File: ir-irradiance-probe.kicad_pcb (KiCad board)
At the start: 4 copper layers, 40 x 40 mm, 59 parts, among them J1 USB-C_UJC-HP-3-SMT-TR, J2 SM04B-SRSS-TB-LF-SN, J3 PinHeader_1x2_P2.54mm_Drill1.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, J4 Conn_BNC_031-70526-21, SW1 MSS3-V-T_R, U1 TLV70033_SC70, U2 AD8604ARUZ, U3 ADC101C027CIMK

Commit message: [47284] Add pcb sha string
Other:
- board text added: "PCB SHA ########"
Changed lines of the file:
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@@
+    (effects (font (size 0.7 0.7) (thickness 0.15)) (justify mirror))
+  )
+  (gr_text "PCB SHA ########" (at 94.39 73.78) (layer "B.SilkS")
     (effects (font (size 0.7 0.7) (thickness 0.15)) (justify mirror))
   )

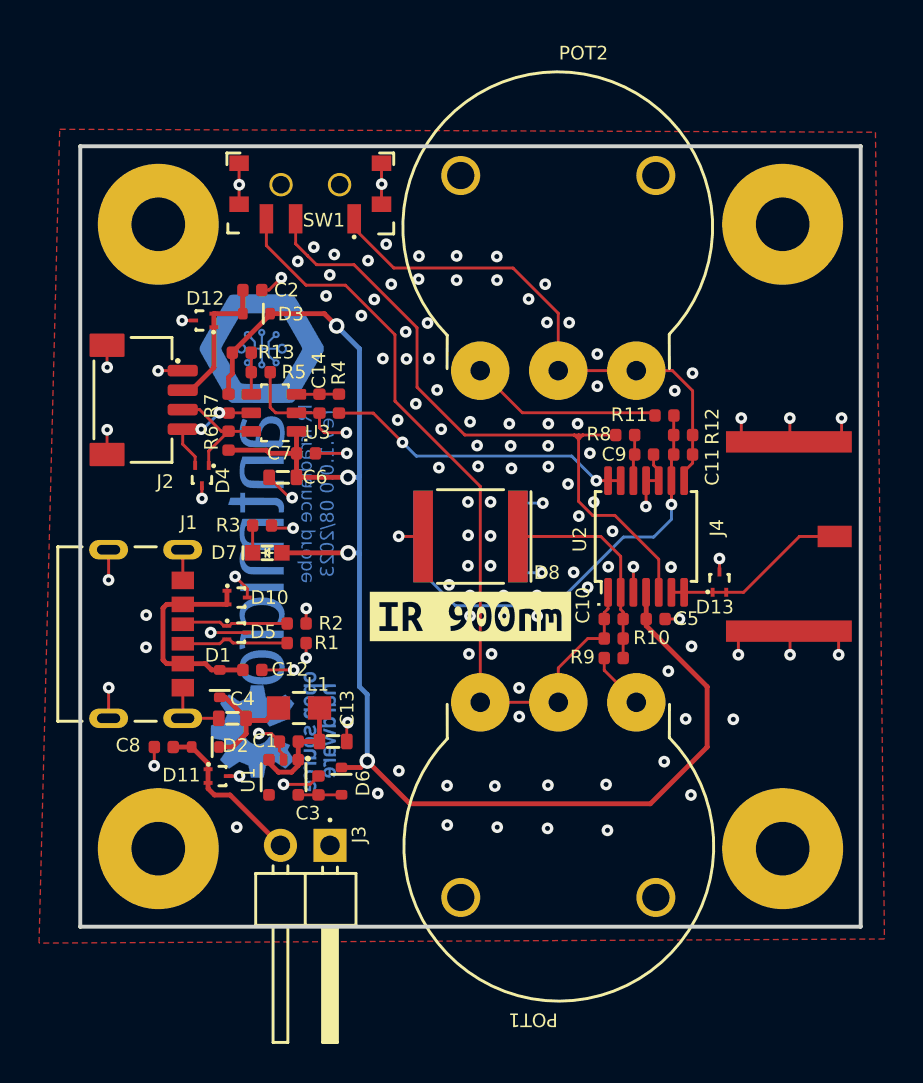
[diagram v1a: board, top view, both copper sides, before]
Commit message: [47284] Add connectors labels
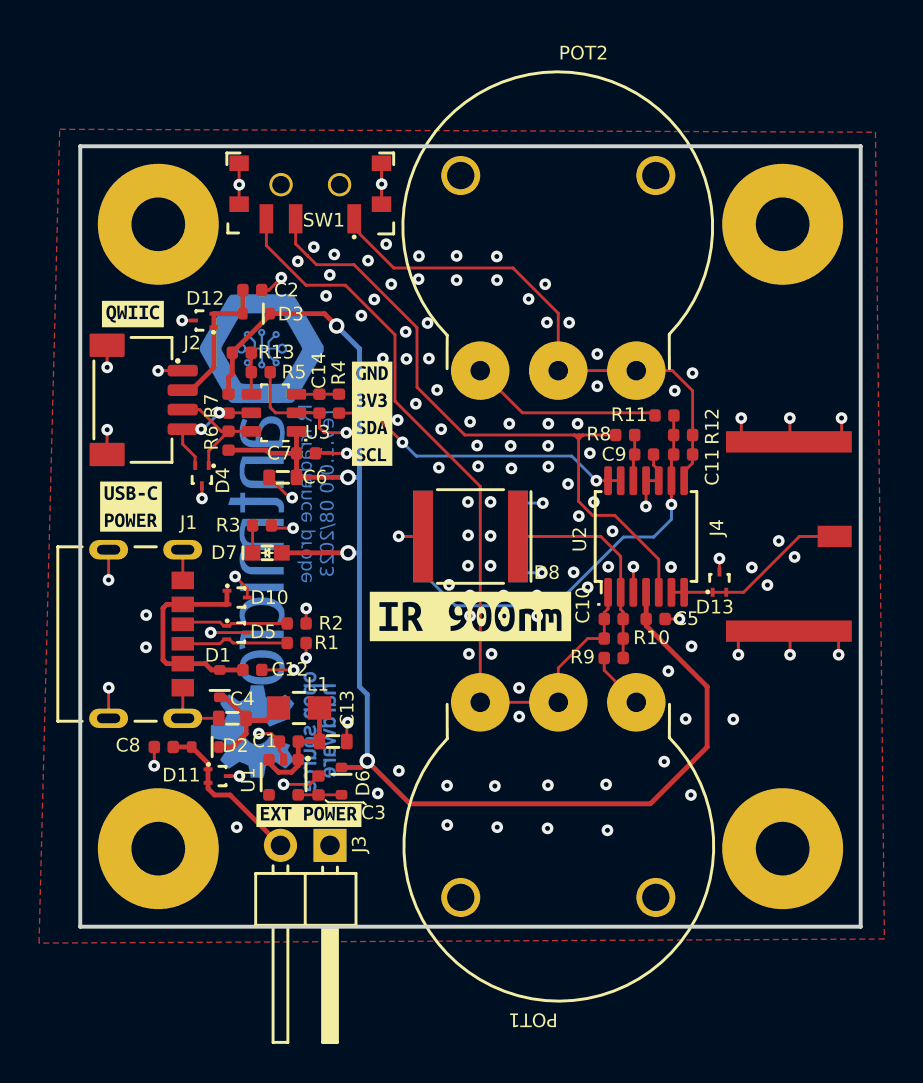
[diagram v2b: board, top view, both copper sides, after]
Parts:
- added kibuzzard-64DA12EE: G***, kibuzzard-64DA12EE, F.Cu at (72.7, 78.6)
- added kibuzzard-64DA1325: G***, kibuzzard-64DA1325, F.Cu at (72.6, 88.5)
- added kibuzzard-64DA143B: G***, kibuzzard-64DA143B, F.Cu at (81.7, 104.3)
- added kibuzzard-64DA14BC: G***, kibuzzard-64DA14BC, F.Cu at (85.0, 83.7)
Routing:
- net GND: vias 127 -> 131

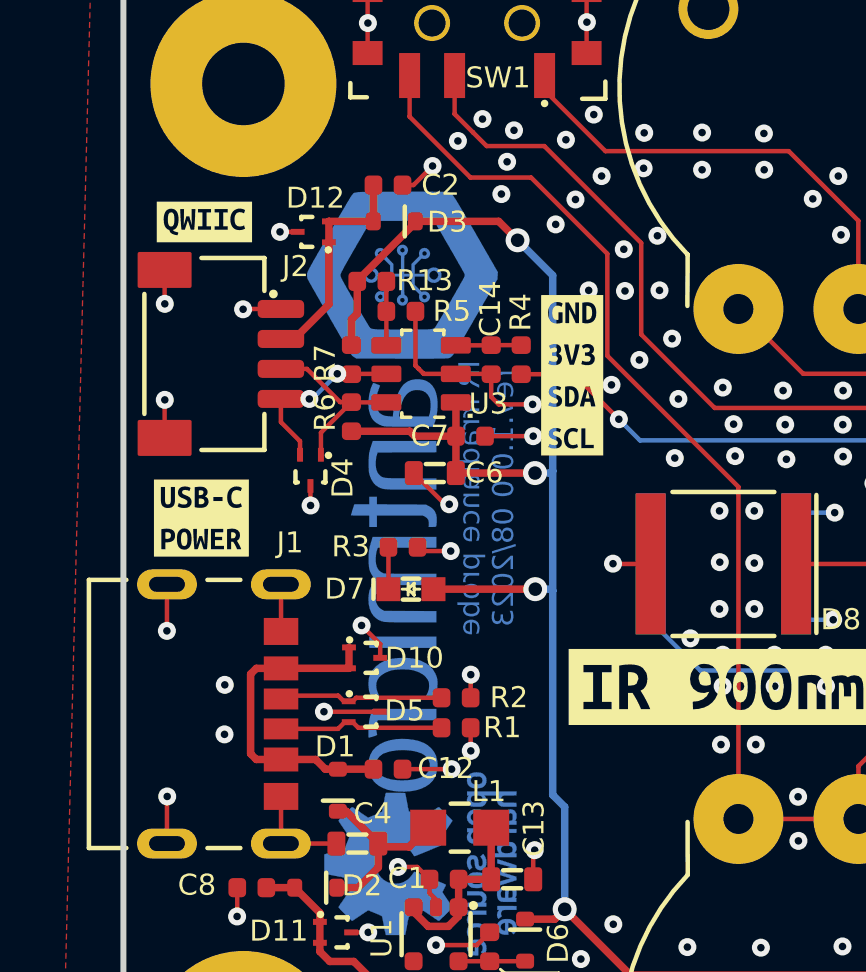
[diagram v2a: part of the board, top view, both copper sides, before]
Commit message: [#47284] Fix antmicro and ohw logos positioning
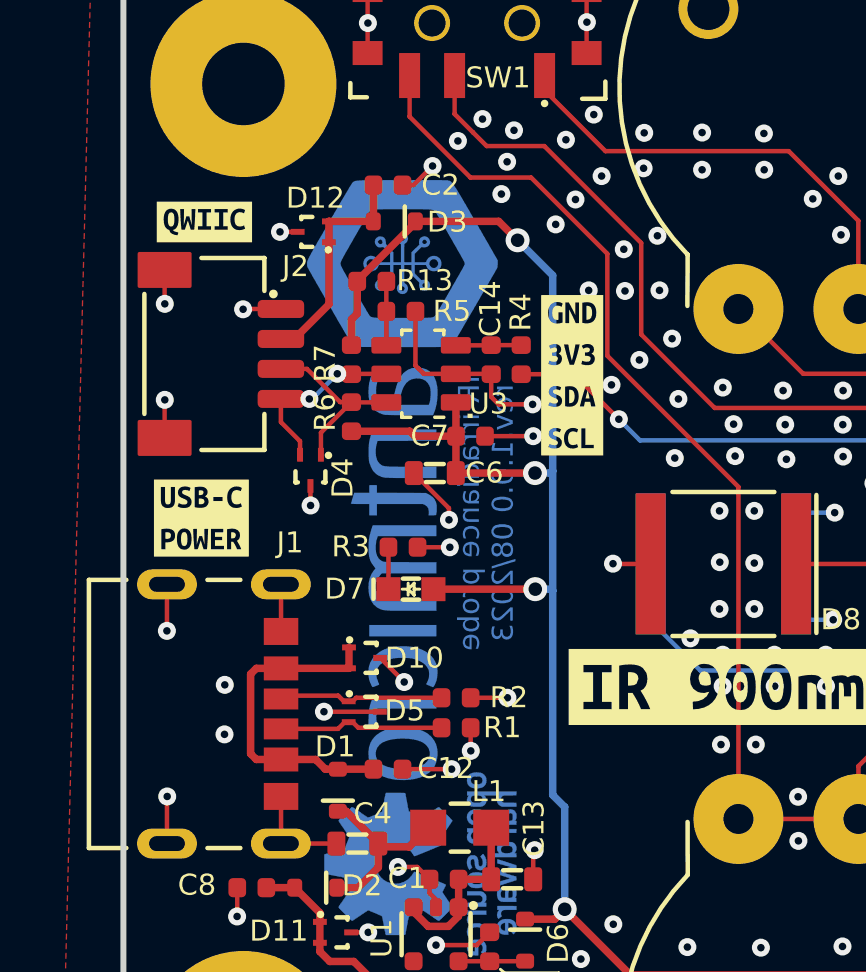
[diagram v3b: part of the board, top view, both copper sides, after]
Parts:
- moved N1 0.39 mm to (79.5, 87.2)
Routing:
- net GND: track 61.3 -> 61.9 mm
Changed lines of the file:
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@@
     (attr board_only exclude_from_pos_files exclude_from_bom)
     (fp_text reference "kibuzzard-64DA1325" (at 0 -4.332869) (layer "F.SilkS") hide
-      (effects (font (size 0 0)))
+      (effects (font (size 0 0) (thickness 0.15)))
     )
     (fp_text value "G***" (at 0 4.332869) (layer "F.SilkS") hide
-      (effects (font (size 0 0)))
+      (effects (font (size 0 0) (thickness 0.15)))
     )
     (fp_poly (pts
@@
     (attr board_only exclude_from_pos_files exclude_from_bom)
     (fp_text reference "kibuzzard-64DA12EE" (at 0 -3.725677) (layer "F.SilkS") hide
-      (effects (font (size 0 0)))
+      (effects (font (size 0 0) (thickness 0.15)))
     )
     (fp_text value "G***" (at 0 3.725677) (layer "F.SilkS") hide
-      (effects (font (size 0 0)))
+      (effects (font (size 0 0) (thickness 0.15)))
     )
     (fp_poly (pts
@@
     (attr board_only exclude_from_pos_files exclude_from_bom)
     (fp_text reference "kibuzzard-64DA143B" (at 0 -3.638444) (layer "F.SilkS") hide
-      (effects (font (size 0 0)))
+      (effects (font (size 0 0) (thickness 0.15)))
     )
     (fp_text value "G***" (at 0 3.638444) (layer "F.SilkS") hide
-      (effects (font (size 0 0)))
+      (effects (font (size 0 0) (thickness 0.15)))
     )
     (fp_poly (pts
@@
     (attr board_only exclude_from_pos_files exclude_from_bom)
     (fp_text reference "kibuzzard-64DA14BC" (at 0 -5.721727) (layer "F.SilkS") hide
-      (effects (font (size 0 0)))
+      (effects (font (size 0 0) (thickness 0.15)))
     )
     (fp_text value "G***" (at 0 5.721727) (layer "F.SilkS") hide
-      (effects (font (size 0 0)))
+      (effects (font (size 0 0) (thickness 0.15)))
     )
     (fp_poly (pts
@@
   )
   (footprint "ir-irradiance-probe-footprints:antmicro-logo_scaled_20mm" (layer "B.Cu")
-    (at 79.489 87.5865 -90)
+    (at 79.489 87.2 -90)
     (property "Author" "Antmicro")
     (property "License" "Apache-2.0")
@@
   (gr_line (start 82.695 103.63) (end 84.51 103.63) (layer "F.SilkS") (width 0.1))
   (gr_rect (start 70 70) (end 110 110) (layer "Edge.Cuts") (width 0.2) (fill none))
-  (gr_text "IR irradiance probe\nrev.1.0.0 08/2023" (at 82.1 87.8 90) (layer "B.Cu")
+  (gr_text "IR irradiance probe\nrev.1.0.0 08/2023" (at 82.09 88.3 90) (layer "B.Cu")
     (effects (font (size 0.7 0.7) (thickness 0.15)) (justify mirror))
   )
@@
     (effects (font (size 0.7 0.7) (thickness 0.15)) (justify mirror))
   )
-  (gr_text "IR irradiance probe\nrev.1.0.0 08/2023" (at 82.1 87.8 90) (layer "B.Mask")
+  (gr_text "IR irradiance probe\nrev.1.0.0 08/2023" (at 82.09 88.3 90) (layer "B.Mask")
     (effects (font (size 0.7 0.7) (thickness 0.15)) (justify mirror))
   )
@@
   (segment (start 79.84 83.49) (end 79.735 83.385) (width 0.15) (layer "F.Cu") (net 1))
   (segment (start 85.44 72.969) (end 85.44 70.869) (width 0.15) (layer "F.Cu") (net 1))
+  (segment (start 80.88136 89.443642) (end 79.808642 89.443642) (width 0.15) (layer "F.Cu") (net 1))
   (segment (start 82.21 102.276) (end 81.7815 102.7045) (width 0.15) (layer "F.Cu") (net 1))
   (segment (start 73.796 101.744) (end 73.79 101.75) (width 0.15) (layer "F.Cu") (net 1))
   (segment (start 99 87.138) (end 99 88.45) (width 0.15) (layer "F.Cu") (net 1))
-  (segment (start 80.862 88.009818) (end 80.719818 88.009818) (width 0.15) (layer "F.Cu") (net 1))
+  (segment (start 80.852145 88.529019) (end 80.852145 88.142145) (width 0.15) (layer "F.Cu") (net 1))
   (segment (start 81.575 95.46) (end 81.575 96.225) (width 0.15) (layer "F.Cu") (net 1))
   (segment (start 79.735 83.385) (end 79.735 81.58) (width 0.15) (layer "F.Cu") (net 1))
@@
   (segment (start 80.206 100.976) (end 80.206 100.51) (width 0.15) (layer "F.Cu") (net 1))
   (segment (start 75.255 99.315) (end 75.25 99.32) (width 0.15) (layer "F.Cu") (net 1))
-  (segment (start 79.935 89.57) (end 79.805 89.44) (width 0.15) (layer "F.Cu") (net 1))
   (segment (start 109.02 85.14) (end 109.02 83.932) (width 0.15) (layer "F.Cu") (net 1))
+  (segment (start 82.8 94.46) (end 81.575 94.46) (width 0.15) (layer "F.Cu") (net 1))
   (segment (start 71.453 99.32) (end 71.453 97.757) (width 0.15) (layer "F.Cu") (net 1))
   (segment (start 75.81 78.93) (end 75.22 78.93) (width 0.15) (layer "F.Cu") (net 1))
-  (segment (start 80.719818 88.009818) (end 79.68 86.97) (width 0.15) (layer "F.Cu") (net 1))
   (segment (start 80.421949 101.442) (end 80.421949 101.191949) (width 0.15) (layer "F.Cu") (net 1))
-  (segment (start 81.575 94.46) (end 81.575 93.695) (width 0.15) (layer "F.Cu") (net 1))
   (segment (start 76.235 88.045) (end 76.24 88.05) (width 0.15) (layer "F.Cu") (net 1))
   (segment (start 106.379 94.851) (end 106.379 96.059) (width 0.15) (layer "F.Cu") (net 1))
+  (segment (start 79.808642 89.443642) (end 79.805 89.44) (width 0.15) (layer "F.Cu") (net 1))
   (segment (start 75.255 92.25) (end 75.255 90.684) (width 0.15) (layer "F.Cu") (net 1))
   (segment (start 99.65 87.138) (end 99.65 86.61) (width 0.15) (layer "F.Cu") (net 1))
@@
   (segment (start 79.84 83.49) (end 80.013 83.663) (width 0.15) (layer "F.Cu") (net 1))
   (segment (start 82.26 84.43) (end 82.51 84.68) (width 0.15) (layer "F.Cu") (net 1))
+  (segment (start 79.36 93.9355) (end 79.36 93.93) (width 0.15) (layer "F.Cu") (net 1))
   (segment (start 82.26 83.674) (end 82.26 84.43) (width 0.15) (layer "F.Cu") (net 1))
   (segment (start 108.869 96.059) (end 108.87 96.06) (width 0.15) (layer "F.Cu") (net 1))
@@
   (segment (start 109.02 83.932) (end 109.019 83.931) (width 0.15) (layer "F.Cu") (net 1))
   (segment (start 99.65 86.61) (end 99.384 86.344) (width 0.15) (layer "F.Cu") (net 1))
+  (segment (start 79.36 93.93) (end 78.56 93.13) (width 0.15) (layer "F.Cu") (net 1))
   (segment (start 75.255 90.684) (end 75.25 90.679) (width 0.15) (layer "F.Cu") (net 1))
   (segment (start 83.66 85.74) (end 82.054 85.74) (width 0.15) (layer "F.Cu") (net 1))
-  (segment (start 80.91 89.57) (end 79.935 89.57) (width 0.15) (layer "F.Cu") (net 1))
   (segment (start 81.7815 102.7045) (end 80.42 102.7045) (width 0.15) (layer "F.Cu") (net 1))
   (segment (start 99.65 87.138) (end 99 87.138) (width 0.15) (layer "F.Cu") (net 1))
@@
   (segment (start 80.013 83.663) (end 81.08 83.663) (width 0.15) (layer "F.Cu") (net 1))
   (segment (start 108.869 94.851) (end 108.869 96.059) (width 0.15) (layer "F.Cu") (net 1))
+  (segment (start 80.852145 88.142145) (end 79.68 86.97) (width 0.15) (layer "F.Cu") (net 1))
   (segment (start 77.59 102.28) (end 78.16 102.28) (width 0.15) (layer "F.Cu") (net 1))
   (segment (start 79.796 100.1) (end 80.206 100.51) (width 0.15) (layer "F.Cu") (net 1))
   (segment (start 71.374 80.199) (end 71.374 81.324) (width 0.15) (layer "F.Cu") (net 1))
-  (segment (start 81.575 93.695) (end 81.58 93.69) (width 0.15) (layer "F.Cu") (net 1))
   (segment (start 80.305 76.735) (end 79.67 77.37) (width 0.15) (layer "F.Cu") (net 1))
   (segment (start 76.685 94.925) (end 78.55 94.925) (width 0.15) (layer "F.Cu") (net 1))
@@
   (segment (start 103.88 83.932) (end 103.879 83.931) (width 0.15) (layer "F.Cu") (net 1))
   (segment (start 79.15 100.1) (end 79.796 100.1) (width 0.15) (layer "F.Cu") (net 1))
-  (segment (start 78.56 92.67) (end 77.94 92.05) (width 0.15) (layer "F.Cu") (net 1))
   (segment (start 79.67 77.37) (end 79.304 77.37) (width 0.15) (layer "F.Cu") (net 1))
   (segment (start 71.374 81.324) (end 71.38 81.33) (width 0.15) (layer "F.Cu") (net 1))
@@
   (segment (start 99.384 86.344) (end 99.384 85.8) (width 0.15) (layer "F.Cu") (net 1))
   (segment (start 106.37 83.932) (end 106.369 83.931) (width 0.15) (layer "F.Cu") (net 1))
-  (segment (start 78.56 93.13) (end 78.56 92.67) (width 0.15) (layer "F.Cu") (net 1))
   (segment (start 83.66 100.51) (end 83.66 99.59) (width 0.15) (layer "F.Cu") (net 1))
   (segment (start 75.255 97.749) (end 75.255 99.315) (width 0.15) (layer "F.Cu") (net 1))
@@
   (via (at 101.38 81.63) (size 0.6) (drill 0.25) (layers "F.Cu" "B.Cu") (free) (net 1))
   (via (at 96.005878 92.605878) (size 0.6) (drill 0.25) (layers "F.Cu" "B.Cu") (free) (net 1))
-  (via (at 80.862 88.009818) (size 0.6) (drill 0.25) (layers "F.Cu" "B.Cu") (net 1))
+  (via (at 80.852145 88.529019) (size 0.6) (drill 0.25) (layers "F.Cu" "B.Cu") (net 1))
   (via (at 85.51 80.88) (size 0.6) (drill 0.25) (layers "F.Cu" "B.Cu") (free) (net 1))
   (via (at 81.97 75.17) (size 0.6) (drill 0.25) (layers "F.Cu" "B.Cu") (free) (net 1))
@@
   (via (at 96.320878 88.239122) (size 0.6) (drill 0.25) (layers "F.Cu" "B.Cu") (free) (net 1))
   (via (at 101.03 99.35) (size 0.6) (drill 0.25) (layers "F.Cu" "B.Cu") (free) (net 1))
-  (via (at 81.58 93.69) (size 0.6) (drill 0.25) (layers "F.Cu" "B.Cu") (net 1))
+  (via (at 82.8 94.46) (size 0.6) (drill 0.25) (layers "F.Cu" "B.Cu") (net 1))
   (via (at 97.02 105.06) (size 0.6) (drill 0.25) (layers "F.Cu" "B.Cu") (free) (net 1))
   (via (at 75.22 78.93) (size 0.6) (drill 0.25) (layers "F.Cu" "B.Cu") (net 1))
@@
   (via (at 81.15 75.9) (size 0.6) (drill 0.25) (layers "F.Cu" "B.Cu") (free) (net 1))
   (via (at 90.34 85.34) (size 0.6) (drill 0.25) (layers "F.Cu" "B.Cu") (free) (net 1))
-  (via (at 80.91 89.57) (size 0.6) (drill 0.25) (layers "F.Cu" "B.Cu") (net 1))
+  (via (at 80.88136 89.443642) (size 0.6) (drill 0.25) (layers "F.Cu" "B.Cu") (net 1))
   (via (at 78.15 71.97) (size 0.6) (drill 0.25) (layers "F.Cu" "B.Cu") (net 1))
   (via (at 93.95 104.96) (size 0.6) (drill 0.25) (layers "F.Cu" "B.Cu") (free) (net 1))
-  (via (at 77.94 92.05) (size 0.6) (drill 0.25) (layers "F.Cu" "B.Cu") (net 1))
+  (via (at 79.36 93.9355) (size 0.6) (drill 0.25) (layers "F.Cu" "B.Cu") (net 1))
   (via (at 89.92 96.02) (size 0.6) (drill 0.25) (layers "F.Cu" "B.Cu") (free) (net 1))
   (via (at 86.33 102.01) (size 0.6) (drill 0.25) (layers "F.Cu" "B.Cu") (free) (net 1))

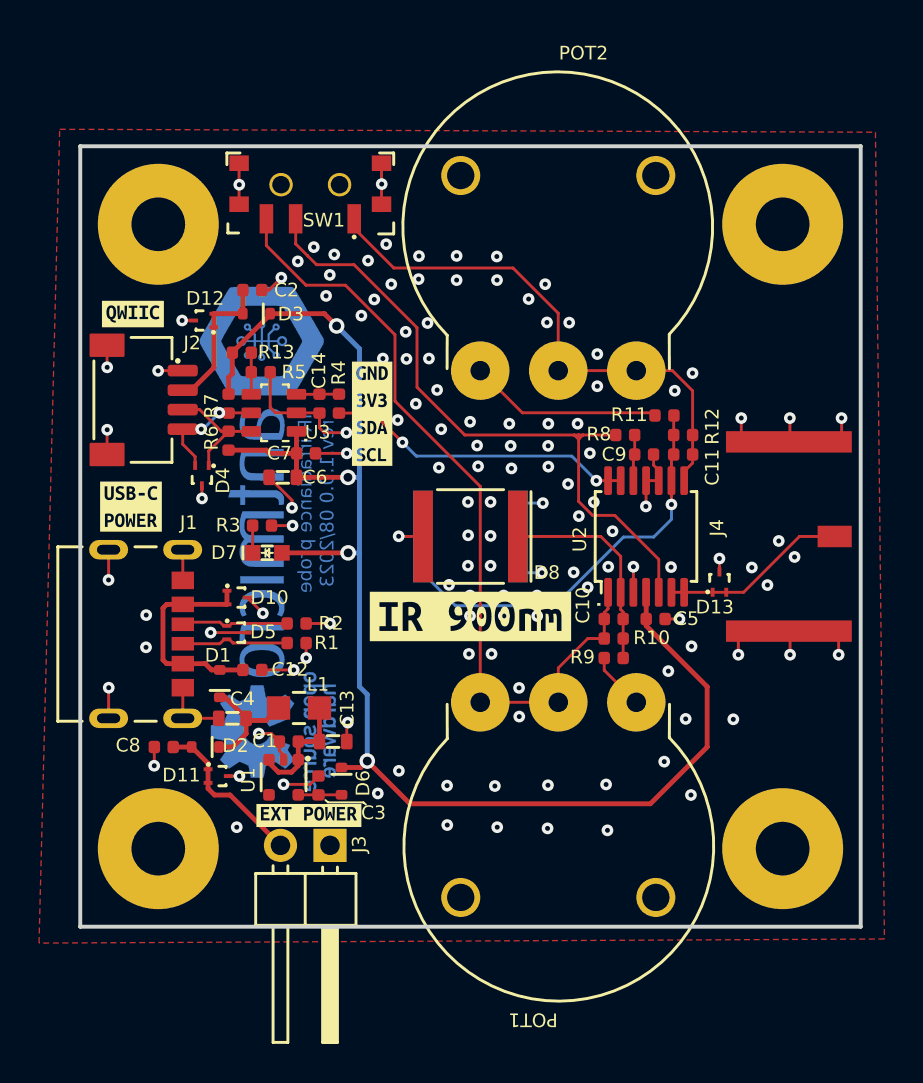
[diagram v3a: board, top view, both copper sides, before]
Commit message: [#47284] Fix routing
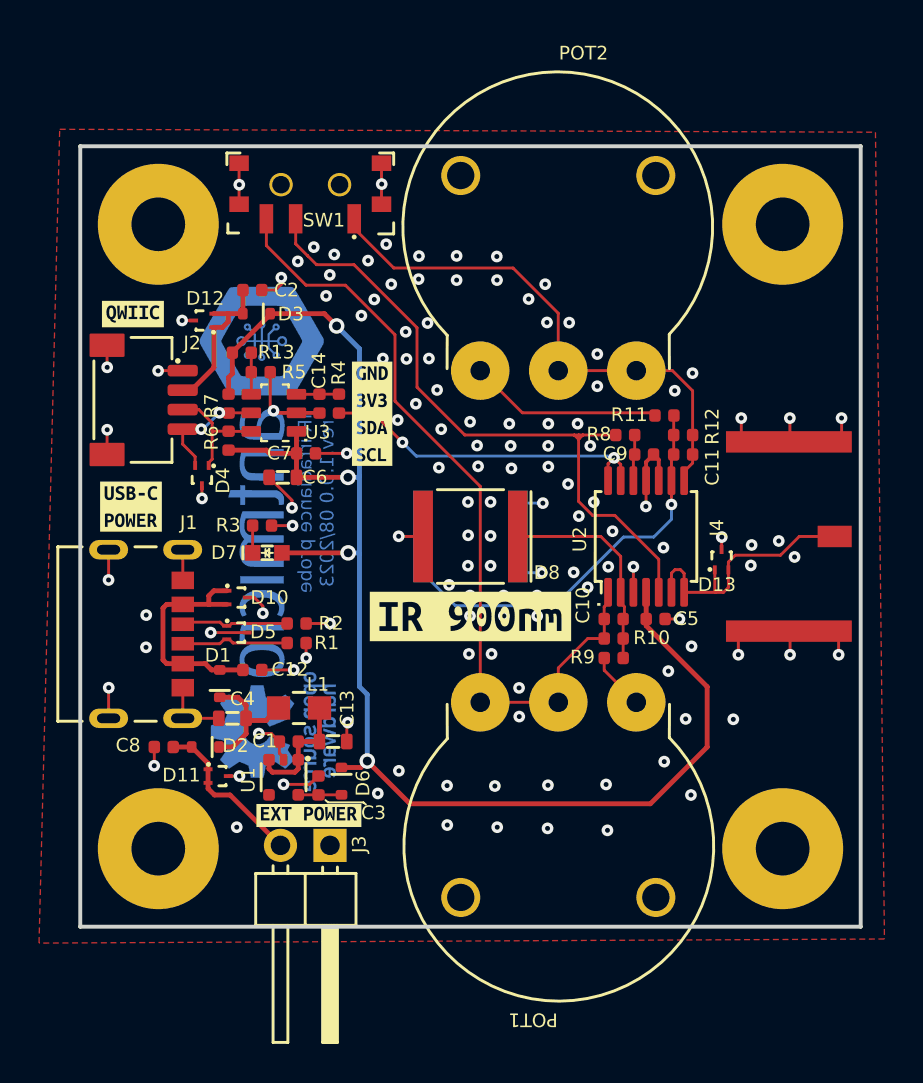
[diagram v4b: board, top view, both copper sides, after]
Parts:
- moved D13 1.16 mm to (102.9, 91.2)
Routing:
- net Net-(D13-Pad1): track 9.61 -> 13.6 mm
- net GND: track 61.9 -> 63.8 mm
- net /ADC_IR_SIG_IN: track 15.9 -> 17.7 mm
- net /5V_USB: track 11.0 -> 11.8 mm
- net /3V3_JST: track 7.54 -> 8.10 mm
